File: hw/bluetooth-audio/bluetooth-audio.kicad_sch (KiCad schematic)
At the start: 0 parts

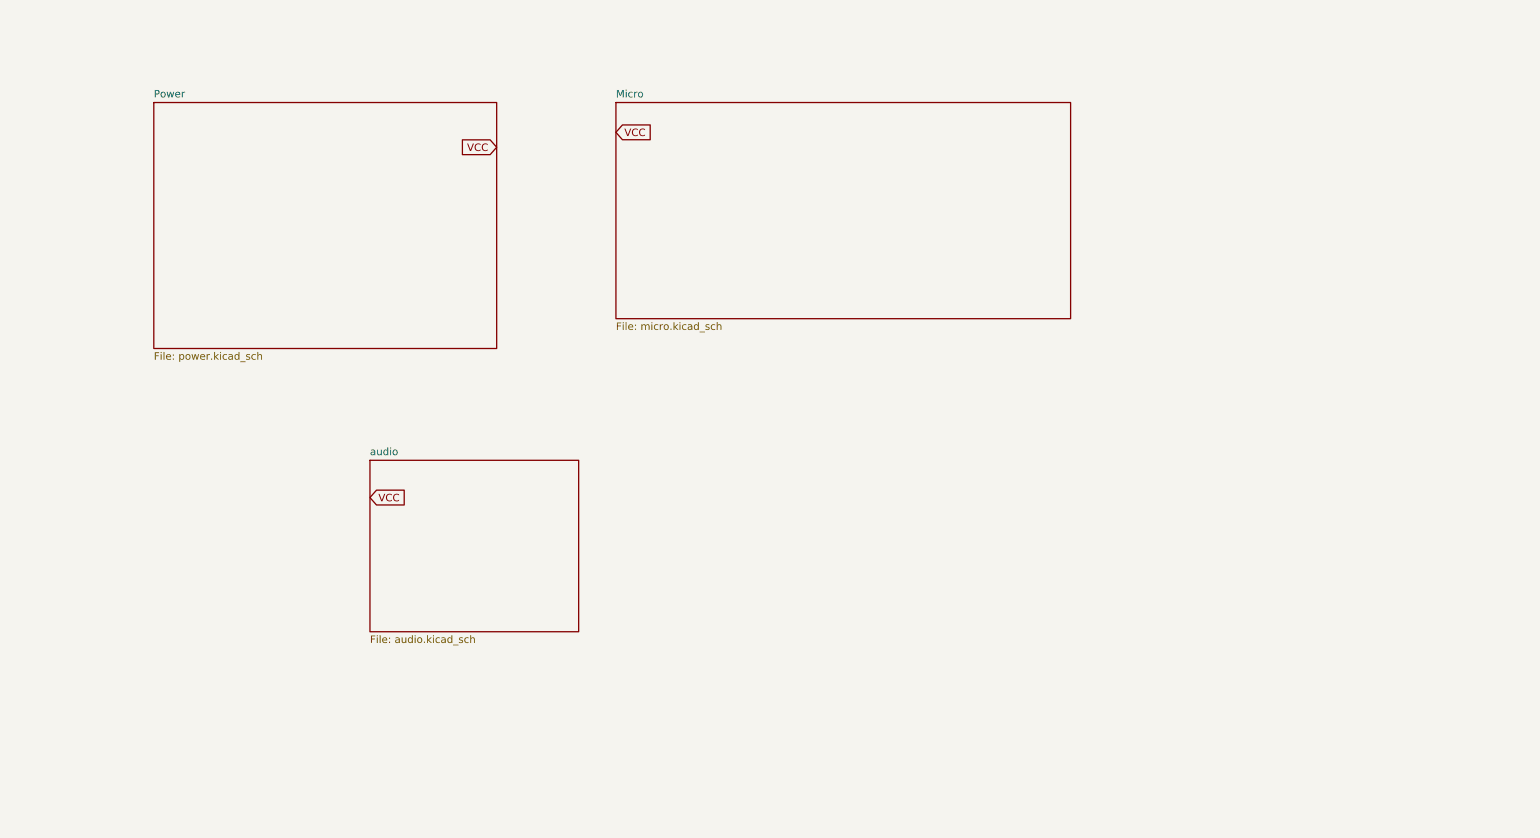
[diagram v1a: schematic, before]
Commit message: Rev B micro sheet: correctness fixes, CH340 load switch, full ESP32 GPIO map
Micro-sheet fixes (netlist-verified):
- UART TX/RX crossover corrected (U0RXD<->CH340 TXD, U0TXD<->CH340 RXD)
- Flash IO2/IO3 uncrossed (GPIO9/SPIWP->IO2, GPIO10/SPIHD->IO3)
- Digital rail unified to +3V3_SYS; EN pull-up (R11) reconnected

CH340K high-side load switch (delta #16):
- Q2 AO3401A (SOT-23, LCSC C15127) + R40 100k gate pull-down = default-ON
  so the ROM bootloader is powered for USB flashing; gate CH340_EN on GPIO21,
  firmware drives high to disable the bridge on battery

Full ESP32 interface wired (see design-overview.md 3.8):
- EN1->16, EN2->17, AUDIO_VCC_EN->4, AUDIO_SW->5, CH340_EN->21, CHARGE_EN->2
- /PGOOD->38, /CHG->32; ADC1 senses BAT_ADC->34, USB_CC1->36, USB_CC2->37,
  USB_VBUS_SENSE->39; GPIO33 spare
- AUDIO_SW drives both TS5A23159 inputs (LOW=RX, HIGH=TX); pinout verified
  against TI datasheet (COM=jack, NC=codec-out, NO=codec-in, both channels)

Docs:
- design-overview.md: committed GPIO map with strapping-pin FW/HW implications
  (3.8), AUDIO_SW/CHARGE_EN firmware notes (9), updated status (10)
- design-review-micro.md: micro-sheet systems review
- added WCH CH340 datasheet; updated TODO
- gitignore MCP snapshot/log artifacts

Co-Authored-By: Claude Opus 4.8 <noreply@anthropic.com>
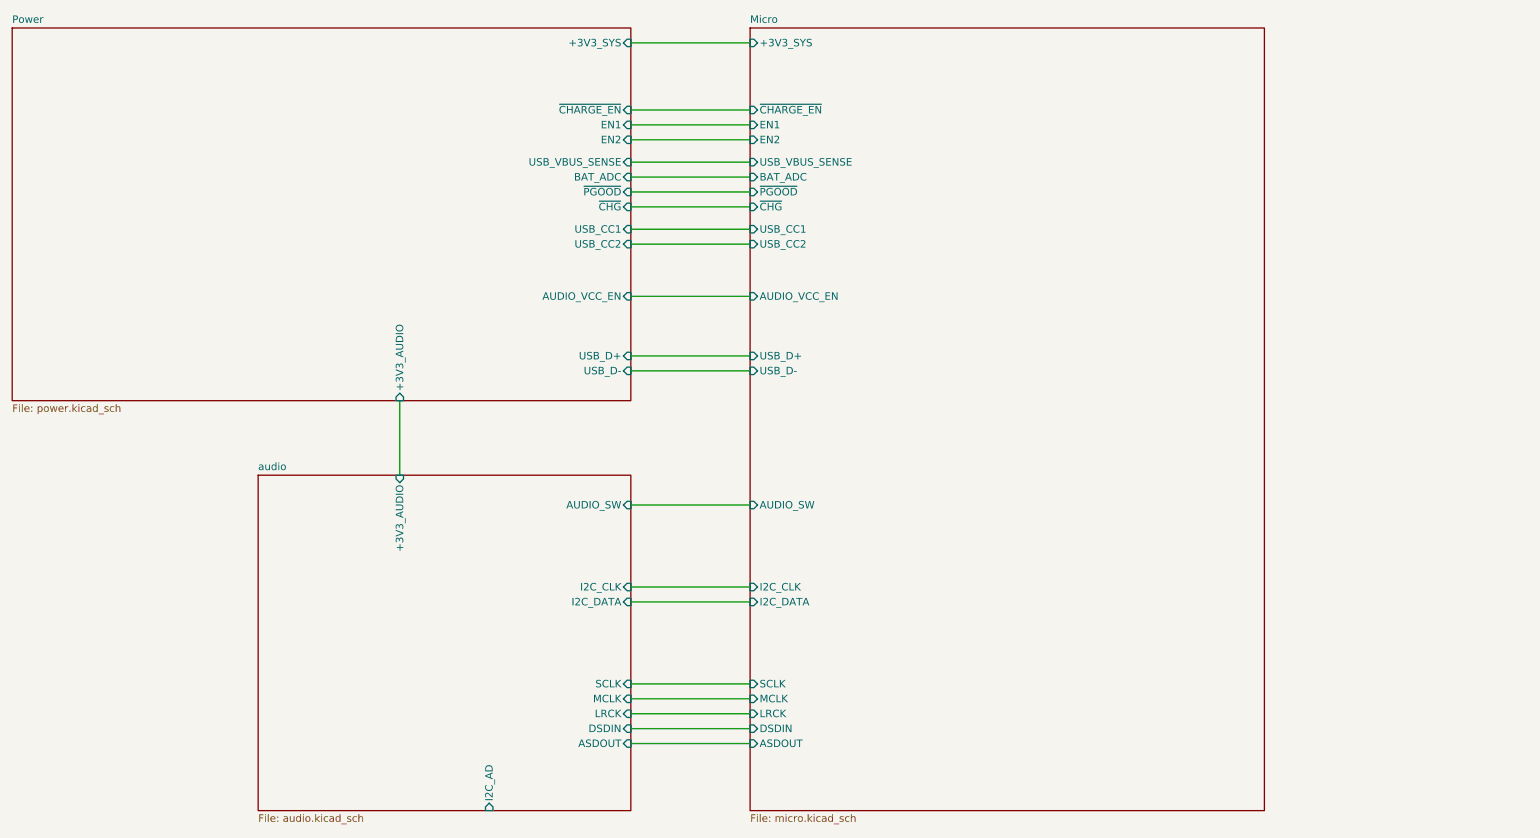
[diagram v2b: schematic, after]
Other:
- sheet Micro ports: added +3V3_SYS, ASDOUT, AUDIO_SW, AUDIO_VCC_EN, BAT_ADC, DSDIN, EN1, EN2, I2C_CLK, I2C_DATA, LRCK, MCLK, SCLK, USB_CC1, USB_CC2, USB_D+, USB_D-, USB_VBUS_SENSE, ~{CHARGE_EN}, ~{CHG}, ~{PGOOD}; removed none
- sheet Power ports: added +3V3_AUDIO, +3V3_SYS, AUDIO_VCC_EN, BAT_ADC, EN1, EN2, USB_CC1, USB_CC2, USB_D+, USB_D-, USB_VBUS_SENSE, ~{CHARGE_EN}, ~{CHG}, ~{PGOOD}; removed none
- sheet audio ports: added +3V3_AUDIO, ASDOUT, AUDIO_SW, DSDIN, I2C_AD, I2C_CLK, I2C_DATA, LRCK, MCLK, SCLK; removed none

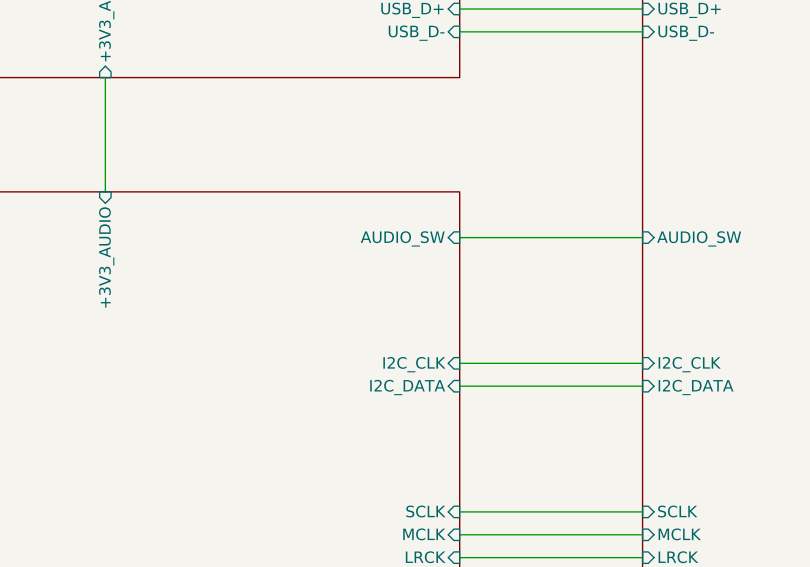
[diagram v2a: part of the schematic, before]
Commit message: Audio sheet redesign: ZTS6216 mic, PJ-3537S jack, shared 47 uF coupling
Rework the audio subsystem and record the rationale.

- Microphone: switch to ZillTek ZTS6216 (self-biased single-ended, C0G
  mic coupling C41/C42 per datasheet); pseudo-diff RIN1 provisioned DNP.
- Jack: PJ-3537S 3-pole TRS + detect switch (custom symbol + footprint).
- Coupling: single shared 47 uF electrolytic pair (C1/C21) on the jack
  side of the TX/RX switch, serving both RX and TX; R22/R23 bleed.
- TX input: BAT54S series-Schottky clamps (D7/D8) to AVDD/GND,
  line-level-only, PGA 0 dB.
- Ground loop: battery-only playback is the plan of record (no
  transformer footprint).
- Add TS5A23159 switch, ZTS6216 and PJ-3537S datasheets.
- Add systems design review (docs/design-review-audio.md) and update
  design overview with coupling-cap sizing.
- PCB layout updated to match.

Co-Authored-By: Claude Opus 4.8 <noreply@anthropic.com>
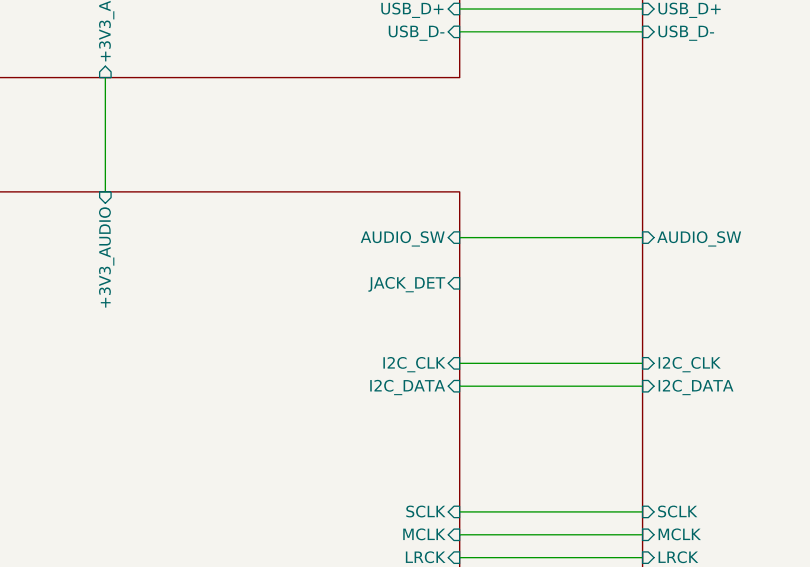
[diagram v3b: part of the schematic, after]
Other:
- sheet audio ports: added JACK_DET; removed none
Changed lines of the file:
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@@
+			)
+		)
+		(pin "JACK_DET" input
+			(at 124.46 110.49 0)
+			(effects
+				(font
+					(size 1.27 1.27)
+				)
+				(justify right)
 			)
 		)

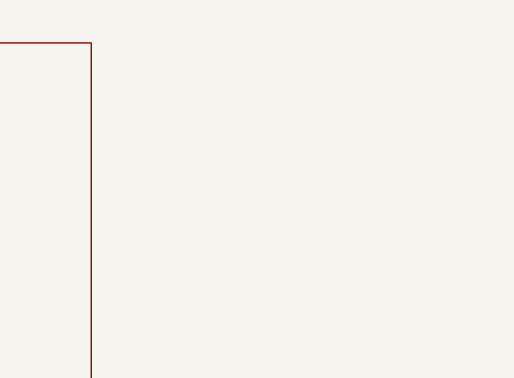
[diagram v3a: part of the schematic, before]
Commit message: Audio BOM: OUT2 couplers to electrolytic, C53 0402, C41/C42 land; place PCB
Schematic (audio + power sheets):
- C24/C26 (ES8388 OUT2 -> TP6 test-output couplers): 1uF MLCC -> 47uF
  electrolytic (Panasonic EEEFT1E470AR / C336270), matching C1/C21. Polarity
  verified against the netlist: + terminal to the codec/VMID side.
- C53 (USB_VBUS_SENSE divider filter): 1206 -> 0402 (house part
  CL05B104KO5NNNC / C1525).
- C41/C42 (mic C0G couplers): footprint aligned to plain C_1206_3216Metric,
  matching C54.

PCB: all footprints now placed in their initial positions, pending V1 routing.

Docs: design-overview.tex updated (delta #20 + 2026-09-16 revision entry). The
D7/D8 TX-input clamp removal is decided but recorded as pending -- that
schematic edit is being done by hand and is not in this commit.

Note: the deleted kicad-library submodule and the untracked in-project library
copies are deliberately left unstaged (broken/redundant state).

Co-Authored-By: Claude Opus 4.8 <noreply@anthropic.com>
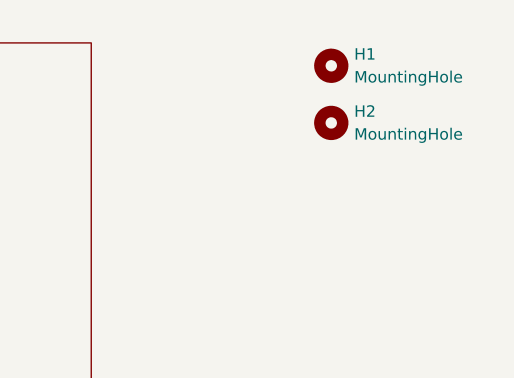
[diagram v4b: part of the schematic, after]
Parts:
- added H1, H2: MountingHole, MountingHole:MountingHole_2.2mm_M2_DIN965_Pad, symbol Mechanical:MountingHole
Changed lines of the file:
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@@
+		)
+	)
+	(symbol
+		(lib_id "Mechanical:MountingHole")
+		(at 259.08 33.02 0)
+		(unit 1)
+		(body_style 1)
+		(exclude_from_sim no)
+		(in_bom no)
+		(on_board yes)
+		(in_pos_files yes)
+		(dnp no)
+		(fields_autoplaced yes)
+		(property "Reference" "H2"
+			(at 261.62 31.7499 0)
+			(show_name no)
+			(do_not_autoplace no)
+			(effects
+				(font
+					(size 1.27 1.27)
+				)
+				(justify left)
+			)
+		)
+		(property "Value" "MountingHole"
+			(at 261.62 34.2899 0)
+			(show_name no)
+			(do_not_autoplace no)
+			(effects
+				(font
+					(size 1.27 1.27)
+				)
+				(justify left)
+			)
+		)
+		(property "Footprint" "MountingHole:MountingHole_2.2mm_M2_DIN965_Pad"
+			(at 259.08 33.02 0)
+			(hide yes)
+			(show_name no)
+			(do_not_autoplace no)
+			(effects
+				(font
+					(size 1.27 1.27)
+				)
+			)
+		)
+		(property "Datasheet" ""
+			(at 259.08 33.02 0)
+			(hide yes)
+			(show_name no)
+			(do_not_autoplace no)
+			(effects
+				(font
+					(size 1.27 1.27)
+				)
+			)
+		)
+		(property "Description" "Mounting Hole without connection"
+			(at 259.08 33.02 0)
+			(hide yes)
+			(show_name no)
+			(do_not_autoplace no)
+			(effects
+				(font
+					(size 1.27 1.27)
+				)
+			)
+		)
+		(instances
+			(project "bluetooth-audio"
+				(path "/eafc8824-f117-40b2-99b0-597946d6c01d"
+					(reference "H2")
+					(unit 1)
+				)
+			)
+		)
+	)
+	(symbol
+		(lib_id "Mechanical:MountingHole")
+		(at 259.08 26.67 0)
+		(unit 1)
+		(body_style 1)
+		(exclude_from_sim no)
+		(in_bom no)
+		(on_board yes)
+		(in_pos_files yes)
+		(dnp no)
+		(fields_autoplaced yes)
+		(property "Reference" "H1"
+			(at 261.62 25.3999 0)
+			(show_name no)
+			(do_not_autoplace no)
+			(effects
+				(font
+					(size 1.27 1.27)
+				)
+				(justify left)
+			)
+		)
+		(property "Value" "MountingHole"
+			(at 261.62 27.9399 0)
+			(show_name no)
+			(do_not_autoplace no)
+			(effects
+				(font
+					(size 1.27 1.27)
+				)
+				(justify left)
+			)
+		)
+		(property "Footprint" "MountingHole:MountingHole_2.2mm_M2_DIN965_Pad"
+			(at 259.08 26.67 0)
+			(hide yes)
+			(show_name no)
+			(do_not_autoplace no)
+			(effects
+				(font
+					(size 1.27 1.27)
+				)
+			)
+		)
+		(property "Datasheet" ""
+			(at 259.08 26.67 0)
+			(hide yes)
+			(show_name no)
+			(do_not_autoplace no)
+			(effects
+				(font
+					(size 1.27 1.27)
+				)
+			)
+		)
+		(property "Description" "Mounting Hole without connection"
+			(at 259.08 26.67 0)
+			(hide yes)
+			(show_name no)
+			(do_not_autoplace no)
+			(effects
+				(font
+					(size 1.27 1.27)
+				)
+			)
+		)
+		(instances
+			(project "bluetooth-audio"
+				(path "/eafc8824-f117-40b2-99b0-597946d6c01d"
+					(reference "H1")
+					(unit 1)
+				)
+			)
 		)
 	)
